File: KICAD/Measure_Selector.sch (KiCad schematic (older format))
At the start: 0 parts

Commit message: labels dans les blocks
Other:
- note added: "Entrées"
- note added: "Sorties"
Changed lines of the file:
@@
 $Descr A4 11693 8268
 encoding utf-8
-Sheet 13 15
+Sheet 12 15
 Title "SESAME"
 Date ""
@@
 Comment4 ""
 $EndDescr
+Text HLabel 5650 4050 0    50   Input ~ 0
+Voltage_Sens_R
+Text HLabel 5650 4150 0    50   Input ~ 0
+Current_Sens_R
+Text HLabel 5650 4350 0    50   Input ~ 0
+Voltage_Sens_L
+Text HLabel 5650 4450 0    50   Input ~ 0
+Current_Sens_L
+Text HLabel 6550 4050 2    50   Output ~ 0
+Voltage_Sens_Selected
+Text HLabel 6550 4150 2    50   Output ~ 0
+Current_Sens_Selected
+Text HLabel 5650 4650 0    50   Input ~ 0
+CC_CV_Mode
+Text HLabel 5650 4750 0    50   Input ~ 0
+Dir
+Text HLabel 6550 4350 2    50   Output ~ 0
+Measure_Selected
+Text Notes 6550 4550 0    50   ~ 0
+Sorties
+Text Notes 5000 4900 0    50   ~ 0
+Entrées
+Wire Notes Line
+	6500 3950 6500 4600
+Wire Notes Line
+	6500 4600 7500 4600
+Wire Notes Line
+	7500 4600 7500 3950
+Wire Notes Line
+	7500 3950 6500 3950
+Wire Notes Line
+	5700 3950 5700 4950
+Wire Notes Line
+	5700 4950 4950 4950
+Wire Notes Line
+	4950 4950 4950 3950
+Wire Notes Line
+	4950 3950 5700 3950
 $EndSCHEMATC

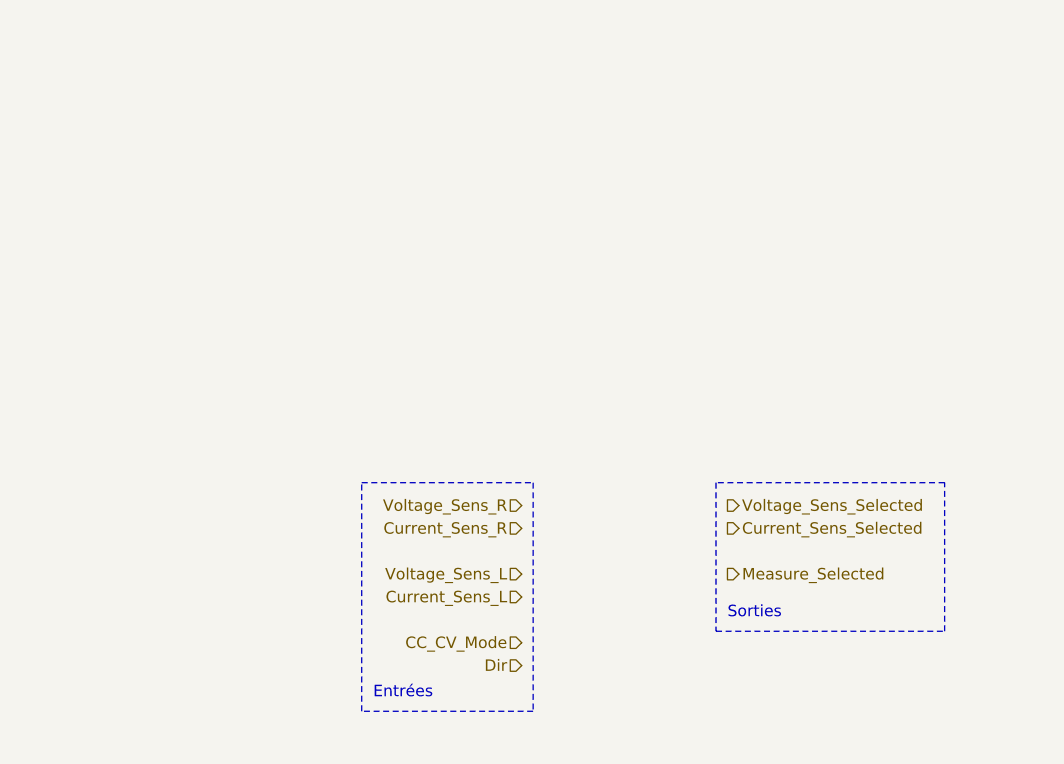
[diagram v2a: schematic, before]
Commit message: add 4053
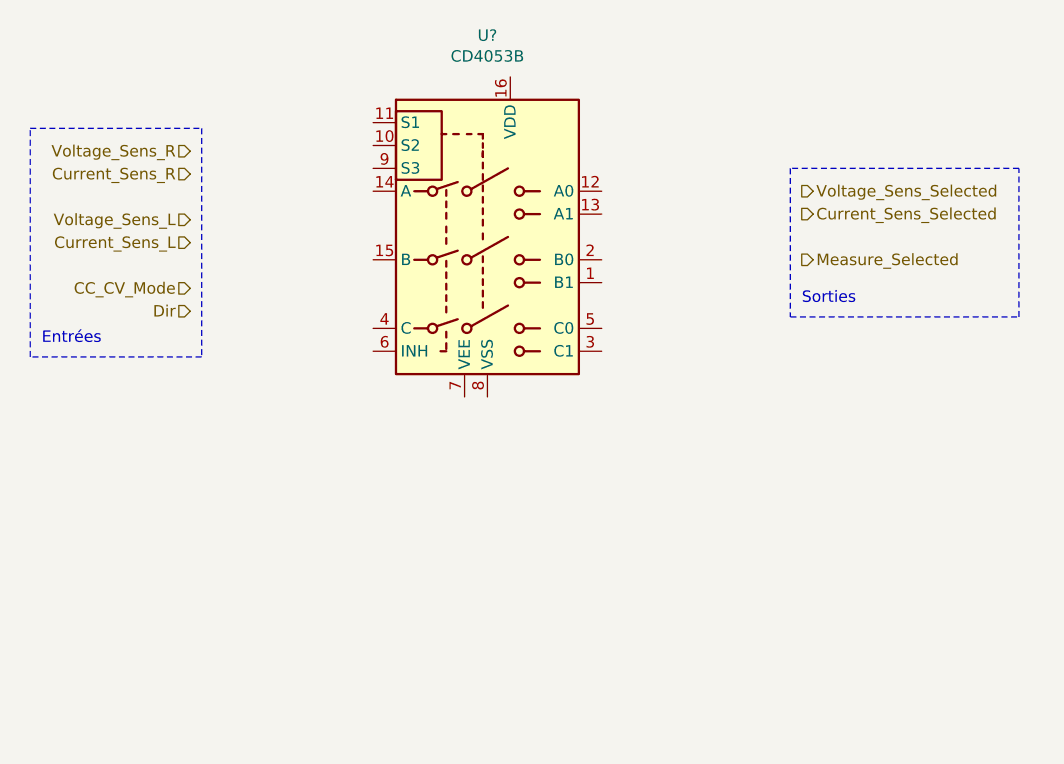
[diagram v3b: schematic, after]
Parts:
- added U?: CD4053B, symbol Analog_Switch:CD4053B
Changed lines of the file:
@@
 Comment4 ""
 $EndDescr
-Text HLabel 5650 4050 0    50   Input ~ 0
+Text HLabel 4200 2500 0    50   Input ~ 0
 Voltage_Sens_R
-Text HLabel 5650 4150 0    50   Input ~ 0
+Text HLabel 4200 2600 0    50   Input ~ 0
 Current_Sens_R
-Text HLabel 5650 4350 0    50   Input ~ 0
+Text HLabel 4200 2800 0    50   Input ~ 0
 Voltage_Sens_L
-Text HLabel 5650 4450 0    50   Input ~ 0
+Text HLabel 4200 2900 0    50   Input ~ 0
 Current_Sens_L
-Text HLabel 6550 4050 2    50   Output ~ 0
+Text HLabel 6875 2675 2    50   Output ~ 0
 Voltage_Sens_Selected
-Text HLabel 6550 4150 2    50   Output ~ 0
+Text HLabel 6875 2775 2    50   Output ~ 0
 Current_Sens_Selected
-Text HLabel 5650 4650 0    50   Input ~ 0
+Text HLabel 4200 3100 0    50   Input ~ 0
 CC_CV_Mode
-Text HLabel 5650 4750 0    50   Input ~ 0
+Text HLabel 4200 3200 0    50   Input ~ 0
 Dir
-Text HLabel 6550 4350 2    50   Output ~ 0
+Text HLabel 6875 2975 2    50   Output ~ 0
 Measure_Selected
-Text Notes 6550 4550 0    50   ~ 0
+Text Notes 6875 3175 0    50   ~ 0
 Sorties
-Text Notes 5000 4900 0    50   ~ 0
+Text Notes 3550 3350 0    50   ~ 0
 Entrées
 Wire Notes Line
-	6500 3950 6500 4600
+	6825 2575 6825 3225
 Wire Notes Line
-	6500 4600 7500 4600
+	6825 3225 7825 3225
 Wire Notes Line
-	7500 4600 7500 3950
+	7825 3225 7825 2575
 Wire Notes Line
-	7500 3950 6500 3950
+	7825 2575 6825 2575
 Wire Notes Line
-	5700 3950 5700 4950
+	4250 2400 4250 3400
 Wire Notes Line
-	5700 4950 4950 4950
+	4250 3400 3500 3400
 Wire Notes Line
-	4950 4950 4950 3950
+	3500 3400 3500 2400
 Wire Notes Line
-	4950 3950 5700 3950
+	3500 2400 4250 2400
+$Comp
+L Analog_Switch:CD4053B U?
+U 1 1 61096CA3
+P 5500 2875
+F 0 "U?" H 5500 3756 50  0000 C CNN
+F 1 "CD4053B" H 5500 3665 50  0000 C CNN
+F 2 "" H 5650 2125 50  0001 L CNN
+F 3 "http://www.ti.com/lit/ds/symlink/cd4052b.pdf" H 5480 3075 50  0001 C CNN
+	1    5500 2875
+	1    0    0    -1
+$EndComp
 $EndSCHEMATC

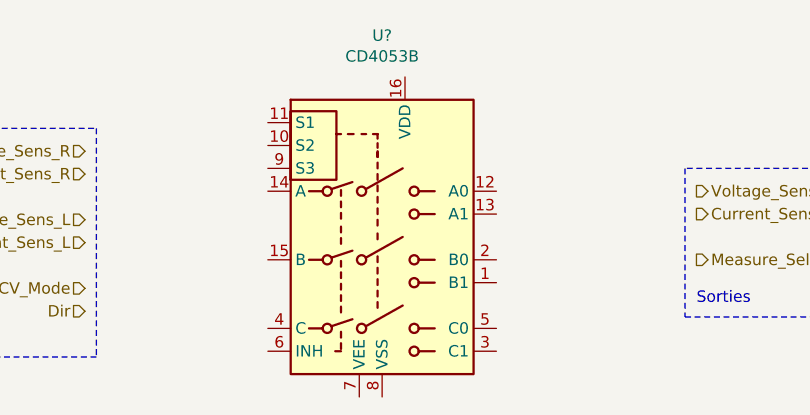
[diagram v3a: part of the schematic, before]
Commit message: fix rescue symbol
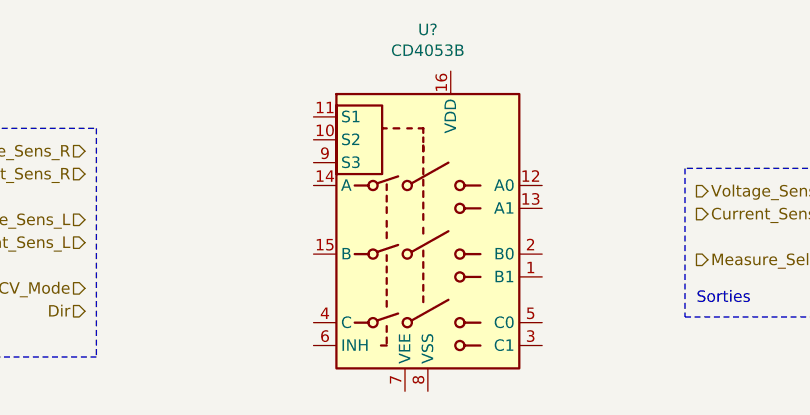
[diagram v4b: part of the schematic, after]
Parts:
- removed U?: CD4053B, symbol Analog_Switch:CD4053B
- added U?: CD4053B, symbol Analog_Switch:CD4053B
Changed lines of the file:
@@
 $Comp
 L Analog_Switch:CD4053B U?
-U 1 1 61096CA3
-P 5500 2875
-F 0 "U?" H 5500 3756 50  0000 C CNN
-F 1 "CD4053B" H 5500 3665 50  0000 C CNN
-F 2 "" H 5650 2125 50  0001 L CNN
-F 3 "http://www.ti.com/lit/ds/symlink/cd4052b.pdf" H 5480 3075 50  0001 C CNN
-	1    5500 2875
+U 1 1 610A09BD
+P 5700 2850
+F 0 "U?" H 5700 3731 50  0000 C CNN
+F 1 "CD4053B" H 5700 3640 50  0000 C CNN
+F 2 "" H 5850 2100 50  0001 L CNN
+F 3 "http://www.ti.com/lit/ds/symlink/cd4052b.pdf" H 5680 3050 50  0001 C CNN
+	1    5700 2850
 	1    0    0    -1
 $EndComp

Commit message: finished measure selector
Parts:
- U?: symbol Analog_Switch:CD4053B -> sesame-fonctionnel-rescue:CD4053B-Analog_Switch
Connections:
- net CC_CV_Mode: now also U?.9 (S3)
- net Current_Sens_L: now also U?.2 (B0)
- net Current_Sens_R: now also U?.1 (B1)
- net Current_Sens_Selected: now also U?.15 (B), U?.3 (C1)
- net Dir: now also U?.10 (S2), U?.11 (S1)
- net Measure_Selected: now also U?.4 (C)
- net Voltage_Sens_L: now also U?.12 (A0)
- net Voltage_Sens_R: now also U?.13 (A1)
- net Voltage_Sens_Selected: now also U?.14 (A), U?.5 (C0)
- net VCC: now reaches U?.16 (VDD)
- net GND: now reaches U?.6 (INH)
- net GND: now also U?.7 (VEE), U?.8 (VSS)
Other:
- note removed: "Entrées"
- note removed: "Sorties"
- moved on the sheet: U?
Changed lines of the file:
@@
 Sheet 12 15
 Title "SESAME"
-Date ""
+Date "2021-08-03"
 Rev ""
 Comp "AFPA"
-Comment1 ""
+Comment1 "Dessin : Clément GRIMARD"
 Comment2 ""
 Comment3 ""
 Comment4 ""
 $EndDescr
-Text HLabel 4200 2500 0    50   Input ~ 0
+Text HLabel 4950 3925 0    50   Input ~ 0
 Voltage_Sens_R
-Text HLabel 4200 2600 0    50   Input ~ 0
+Text HLabel 4950 4225 0    50   Input ~ 0
 Current_Sens_R
-Text HLabel 4200 2800 0    50   Input ~ 0
+Text HLabel 4950 3825 0    50   Input ~ 0
 Voltage_Sens_L
-Text HLabel 4200 2900 0    50   Input ~ 0
+Text HLabel 4950 4125 0    50   Input ~ 0
 Current_Sens_L
-Text HLabel 6875 2675 2    50   Output ~ 0
+Text HLabel 6700 3825 2    50   Output ~ 0
 Voltage_Sens_Selected
-Text HLabel 6875 2775 2    50   Output ~ 0
+Text HLabel 6700 4125 2    50   Output ~ 0
 Current_Sens_Selected
-Text HLabel 4200 3100 0    50   Input ~ 0
+Text HLabel 6700 3725 2    50   Input ~ 0
 CC_CV_Mode
-Text HLabel 4200 3200 0    50   Input ~ 0
+Text HLabel 6700 3575 2    50   Input ~ 0
 Dir
-Text HLabel 6875 2975 2    50   Output ~ 0
+Text HLabel 6700 4425 2    50   Output ~ 0
 Measure_Selected
-Text Notes 6875 3175 0    50   ~ 0
-Sorties
-Text Notes 3550 3350 0    50   ~ 0
-Entrées
-Wire Notes Line
-	6825 2575 6825 3225
-Wire Notes Line
-	6825 3225 7825 3225
-Wire Notes Line
-	7825 3225 7825 2575
-Wire Notes Line
-	7825 2575 6825 2575
-Wire Notes Line
-	4250 2400 4250 3400
-Wire Notes Line
-	4250 3400 3500 3400
-Wire Notes Line
-	3500 3400 3500 2400
-Wire Notes Line
-	3500 2400 4250 2400
 $Comp
-L Analog_Switch:CD4053B U?
+L sesame-fonctionnel-rescue:CD4053B-Analog_Switch U?
 U 1 1 610A09BD
-P 5700 2850
-F 0 "U?" H 5700 3731 50  0000 C CNN
-F 1 "CD4053B" H 5700 3640 50  0000 C CNN
-F 2 "" H 5850 2100 50  0001 L CNN
-F 3 "http://www.ti.com/lit/ds/symlink/cd4052b.pdf" H 5680 3050 50  0001 C CNN
-	1    5700 2850
+P 5775 4025
+AR Path="/610A09BD" Ref="U?"  Part="1"
+AR Path="/60F421D1/610A09BD" Ref="U?"  Part="1"
+F 0 "U?" H 5625 4900 50  0000 C CNN
+F 1 "CD4053B" H 5600 4800 50  0000 C CNN
+F 2 "" H 5925 3275 50  0001 L CNN
+F 3 "http://www.ti.com/lit/ds/symlink/cd4052b.pdf" H 5755 4225 50  0001 C CNN
+	1    5775 4025
+	-1   0    0    -1
+$EndComp
+Wire Wire Line
+	4950 3825 5275 3825
+Wire Wire Line
+	4950 3925 5275 3925
+Wire Wire Line
+	4950 4125 5275 4125
+Wire Wire Line
+	4950 4225 5275 4225
+$Comp
+L power:GND #PWR?
+U 1 1 610C24DF
+P 5825 4875
+F 0 "#PWR?" H 5825 4625 50  0001 C CNN
+F 1 "GND" H 5830 4702 50  0000 C CNN
+F 2 "" H 5825 4875 50  0001 C CNN
+F 3 "" H 5825 4875 50  0001 C CNN
+	1    5825 4875
 	1    0    0    -1
 $EndComp
+Wire Wire Line
+	5775 4725 5775 4800
+Wire Wire Line
+	5875 4800 5875 4725
+Wire Wire Line
+	5775 4800 5825 4800
+Wire Wire Line
+	5825 4800 5825 4875
+Connection ~ 5825 4800
+Wire Wire Line
+	5825 4800 5875 4800
+$Comp
+L power:VCC #PWR?
+U 1 1 610C511E
+P 5675 3200
+F 0 "#PWR?" H 5675 3050 50  0001 C CNN
+F 1 "VCC" H 5692 3373 50  0000 C CNN
+F 2 "" H 5675 3200 50  0001 C CNN
+F 3 "" H 5675 3200 50  0001 C CNN
+	1    5675 3200
+	1    0    0    -1
+$EndComp
+Wire Wire Line
+	5675 3325 5675 3200
+Wire Wire Line
+	6275 3525 6475 3525
+Wire Wire Line
+	6475 3525 6475 3575
+Wire Wire Line
+	6475 3625 6275 3625
+Wire Wire Line
+	6475 3575 6700 3575
+Connection ~ 6475 3575
+Wire Wire Line
+	6475 3575 6475 3625
+Wire Wire Line
+	6700 3725 6275 3725
+Wire Wire Line
+	6275 3825 6700 3825
+Wire Wire Line
+	6275 4425 6700 4425
+Wire Wire Line
+	6275 4125 6700 4125
+Text Label 6325 3825 0    50   ~ 0
+Volt_Sel
+Text Label 6325 4125 0    50   ~ 0
+Curr_Sel
+Text Label 4950 4425 0    50   ~ 0
+Volt_Sel
+Text Label 4950 4525 0    50   ~ 0
+Curr_Sel
+Wire Wire Line
+	4950 4525 5275 4525
+Wire Wire Line
+	4950 4425 5275 4425
+$Comp
+L power:GND #PWR?
+U 1 1 610E2D38
+P 6325 4575
+F 0 "#PWR?" H 6325 4325 50  0001 C CNN
+F 1 "GND" H 6330 4402 50  0000 C CNN
+F 2 "" H 6325 4575 50  0001 C CNN
+F 3 "" H 6325 4575 50  0001 C CNN
+	1    6325 4575
+	1    0    0    -1
+$EndComp
+Wire Wire Line
+	6275 4525 6325 4525
+Wire Wire Line
+	6325 4525 6325 4575
 $EndSCHEMATC
